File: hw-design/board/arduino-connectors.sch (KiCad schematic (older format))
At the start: 11 parts, among them P1 CONN_01X08, P2 CONN_01X06, P3 CONN_01X10, P4 CONN_01X08, Q1 2N7002

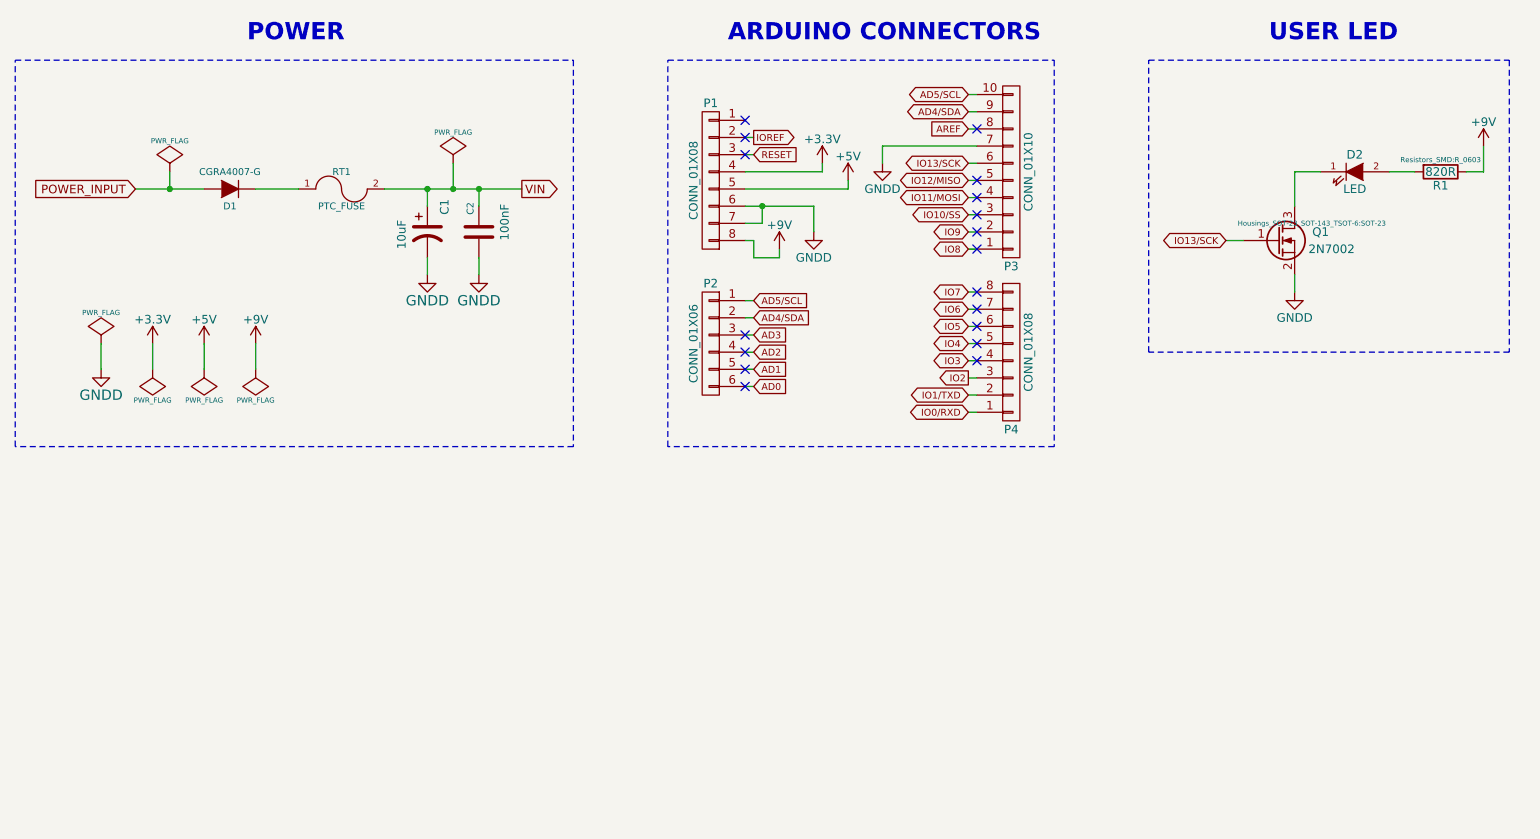
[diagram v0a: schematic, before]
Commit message: sch: setting up footprints
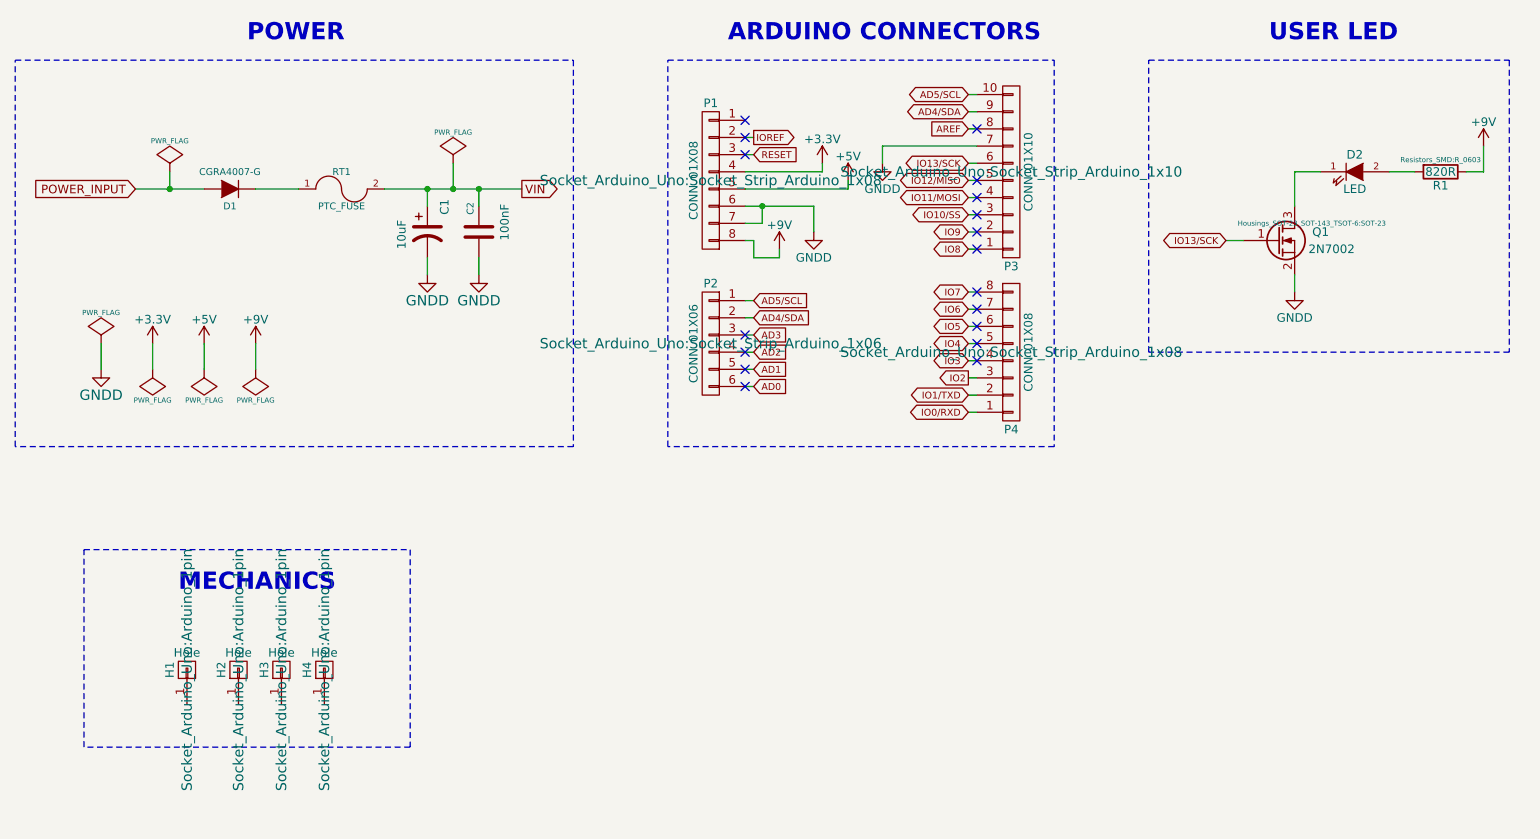
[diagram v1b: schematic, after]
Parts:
- added H1, H2, H3, H4: Hole, Socket_Arduino_Uno:Arduino_1pin, symbol CONN_01X01
- P1, P4: footprint (none) -> Socket_Arduino_Uno:Socket_Strip_Arduino_1x08
- P2: footprint (none) -> Socket_Arduino_Uno:Socket_Strip_Arduino_1x06
- P3: footprint (none) -> Socket_Arduino_Uno:Socket_Strip_Arduino_1x10
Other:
- note added: "MECHANICS"
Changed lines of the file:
@@
 	2800 2050 3050 2050
 Wire Wire Line
-	2100 2050 2300 2050
-Wire Wire Line
-	2300 2050 2500 2050
+	2100 2050 2500 2050
 Wire Wire Line
 	1900 2950 1900 3100
@@
 VIN
 Wire Wire Line
-	3550 2050 3800 2050
-Wire Wire Line
-	3800 2050 3950 2050
-Wire Wire Line
-	3950 2050 4100 2050
-Wire Wire Line
-	4100 2050 4350 2050
+	3550 2050 4350 2050
 NoConn ~ 5650 1650
 Text GLabel 5700 3200 2    40   Input ~ 0
@@
 F 0 "P1" H 5450 2450 50  0000 C CNN
 F 1 "CONN_01X08" V 5550 2000 50  0000 C CNN
-F 2 "" H 5450 2000 60  0000 C CNN
+F 2 "Socket_Arduino_Uno:Socket_Strip_Arduino_1x08" H 5450 2000 60  0000 C CNN
 F 3 "" H 5450 2000 60  0000 C CNN
 	1    5450 2000
@@
 F 0 "P2" H 5450 3300 50  0000 C CNN
 F 1 "CONN_01X06" V 5550 2950 50  0000 C CNN
-F 2 "" H 5450 2950 60  0000 C CNN
+F 2 "Socket_Arduino_Uno:Socket_Strip_Arduino_1x06" H 5450 2950 60  0000 C CNN
 F 3 "" H 5450 2950 60  0000 C CNN
 	1    5450 2950
@@
 F 0 "P3" H 7200 2500 50  0000 C CNN
 F 1 "CONN_01X10" V 7300 1950 50  0000 C CNN
-F 2 "" H 7200 1950 60  0000 C CNN
+F 2 "Socket_Arduino_Uno:Socket_Strip_Arduino_1x10" H 7200 1950 60  0000 C CNN
 F 3 "" H 7200 1950 60  0000 C CNN
 	1    7200 1950
@@
 F 0 "P4" H 7200 3450 50  0000 C CNN
 F 1 "CONN_01X08" V 7300 3000 50  0000 C CNN
-F 2 "" H 7200 3000 60  0000 C CNN
+F 2 "Socket_Arduino_Uno:Socket_Strip_Arduino_1x08" H 7200 3000 60  0000 C CNN
 F 3 "" H 7200 3000 60  0000 C CNN
 	1    7200 3000
@@
 	6050 2150 6050 2300
 Wire Wire Line
-	5650 2150 5750 2150
-Wire Wire Line
-	5750 2150 6050 2150
+	5650 2150 6050 2150
 Wire Wire Line
 	5650 2250 5750 2250
@@
 Wire Wire Line
 	6100 1950 6100 1900
+Text Notes 2350 4400 0    100  ~ 20
+MECHANICS
+$Comp
+L CONN_01X01 H1
+U 1 1 558C38D7
+P 2400 4850
+F 0 "H1" H 2400 4950 50  0000 C CNN
+F 1 "Hole" V 2500 4850 50  0000 C CNN
+F 2 "Socket_Arduino_Uno:Arduino_1pin" H 2400 4850 60  0000 C CNN
+F 3 "" H 2400 4850 60  0000 C CNN
+	1    2400 4850
+	0    -1   -1   0
+$EndComp
+$Comp
+L CONN_01X01 H2
+U 1 1 558C3F79
+P 2700 4850
+F 0 "H2" H 2700 4950 50  0000 C CNN
+F 1 "Hole" V 2800 4850 50  0000 C CNN
+F 2 "Socket_Arduino_Uno:Arduino_1pin" H 2700 4850 60  0000 C CNN
+F 3 "" H 2700 4850 60  0000 C CNN
+	1    2700 4850
+	0    -1   -1   0
+$EndComp
+$Comp
+L CONN_01X01 H3
+U 1 1 558C3FB1
+P 2950 4850
+F 0 "H3" H 2950 4950 50  0000 C CNN
+F 1 "Hole" V 3050 4850 50  0000 C CNN
+F 2 "Socket_Arduino_Uno:Arduino_1pin" H 2950 4850 60  0000 C CNN
+F 3 "" H 2950 4850 60  0000 C CNN
+	1    2950 4850
+	0    -1   -1   0
+$EndComp
+$Comp
+L CONN_01X01 H4
+U 1 1 558C3FE5
+P 3200 4850
+F 0 "H4" H 3200 4950 50  0000 C CNN
+F 1 "Hole" V 3300 4850 50  0000 C CNN
+F 2 "Socket_Arduino_Uno:Arduino_1pin" H 3200 4850 60  0000 C CNN
+F 3 "" H 3200 4850 60  0000 C CNN
+	1    3200 4850
+	0    -1   -1   0
+$EndComp
+Wire Notes Line
+	1800 4150 3700 4150
+Wire Notes Line
+	3700 4150 3700 5300
+Wire Notes Line
+	3700 5300 1800 5300
+Wire Notes Line
+	1800 5300 1800 4150
 $EndSCHEMATC

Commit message: adding footprint to local project directory (submodule)
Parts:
- D2: footprint (none) -> LEDs:LED-0603; MPN (none) -> LS Q976-NR-1
- P1: value CONN_01X08 -> Power
- P2: value CONN_01X06 -> Analog
- P3: value CONN_01X10 -> Digital
- P4: value CONN_01X08 -> Digital
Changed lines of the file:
@@
 U 1 1 548B665F
 P 4100 2300
-F 0 "C2" V 4050 2400 40  0000 L CNN
+F 0 "C2" V 4050 2400 50  0000 L CNN
 F 1 "100nF" V 4250 2250 50  0000 L CNN
 F 2 "Capacitors_SMD:C_0603" H 4138 2150 30  0001 C CNN
@@
 P 5450 2000
 F 0 "P1" H 5450 2450 50  0000 C CNN
-F 1 "CONN_01X08" V 5550 2000 50  0000 C CNN
-F 2 "Socket_Arduino_Uno:Socket_Strip_Arduino_1x08" H 5450 2000 60  0000 C CNN
+F 1 "Power" V 5550 2000 50  0000 C CNN
+F 2 "Socket_Arduino_Uno:Socket_Strip_Arduino_1x08" V 5450 2000 60  0001 C CNN
 F 3 "" H 5450 2000 60  0000 C CNN
 	1    5450 2000
@@
 P 5450 2950
 F 0 "P2" H 5450 3300 50  0000 C CNN
-F 1 "CONN_01X06" V 5550 2950 50  0000 C CNN
-F 2 "Socket_Arduino_Uno:Socket_Strip_Arduino_1x06" H 5450 2950 60  0000 C CNN
+F 1 "Analog" V 5550 2950 50  0000 C CNN
+F 2 "Socket_Arduino_Uno:Socket_Strip_Arduino_1x06" V 5450 2950 60  0001 C CNN
 F 3 "" H 5450 2950 60  0000 C CNN
 	1    5450 2950
@@
 P 7200 1950
 F 0 "P3" H 7200 2500 50  0000 C CNN
-F 1 "CONN_01X10" V 7300 1950 50  0000 C CNN
-F 2 "Socket_Arduino_Uno:Socket_Strip_Arduino_1x10" H 7200 1950 60  0000 C CNN
+F 1 "Digital" V 7300 1950 50  0000 C CNN
+F 2 "Socket_Arduino_Uno:Socket_Strip_Arduino_1x10" V 7200 1950 60  0001 C CNN
 F 3 "" H 7200 1950 60  0000 C CNN
 	1    7200 1950
@@
 P 7200 3000
 F 0 "P4" H 7200 3450 50  0000 C CNN
-F 1 "CONN_01X08" V 7300 3000 50  0000 C CNN
-F 2 "Socket_Arduino_Uno:Socket_Strip_Arduino_1x08" H 7200 3000 60  0000 C CNN
+F 1 "Digital" V 7300 3000 50  0000 C CNN
+F 2 "Socket_Arduino_Uno:Socket_Strip_Arduino_1x08" V 7200 3000 60  0001 C CNN
 F 3 "" H 7200 3000 60  0000 C CNN
 	1    7200 3000
@@
 F 0 "Q1" H 9050 2400 50  0000 R CNN
 F 1 "2N7002" H 9200 2300 50  0000 R CNN
-F 2 "Housings_SOT-23_SOT-143_TSOT-6:SOT-23" H 8950 2450 29  0000 C CNN
+F 2 "Housings_SOT-23_SOT-143_TSOT-6:SOT-23" H 8950 2450 50  0000 C CNN
 F 3 "" H 8750 2350 60  0000 C CNN
 F 4 "2N7002P,215" H 8750 2350 60  0001 C CNN "MPN"
@@
 F 0 "D2" H 9200 2050 50  0000 C CNN
 F 1 "LED" H 9200 1850 50  0000 C CNN
-F 2 "" H 9200 1950 60  0000 C CNN
+F 2 "LEDs:LED-0603" H 9200 2150 50  0000 C CNN
 F 3 "" H 9200 1950 60  0000 C CNN
+F 4 "LS Q976-NR-1" H 9200 1950 60  0001 C CNN "MPN"
 	1    9200 1950
 	1    0    0    -1
@@
 F 0 "R1" V 9780 1950 50  0000 C CNN
 F 1 "820R" V 9700 1950 50  0000 C CNN
-F 2 "Resistors_SMD:R_0603" V 9630 1950 30  0000 C CNN
+F 2 "Resistors_SMD:R_0603" V 9630 1950 50  0000 C CNN
 F 3 "" H 9700 1950 30  0000 C CNN
 F 4 "ESR03EZPJ821" V 9700 1950 60  0001 C CNN "MPN"
@@
 	5850 2450 5850 2400
 $Comp
-L +5V #PWR?
+L +5V #PWR018
 U 1 1 558D2AB4
 P 6250 2000
-F 0 "#PWR?" H 6250 1850 50  0001 C CNN
+F 0 "#PWR018" H 6250 1850 50  0001 C CNN
 F 1 "+5V" H 6250 2140 50  0000 C CNN
 F 2 "" H 6250 2000 60  0000 C CNN
@@
 	6250 2050 6250 2000
 $Comp
-L +3.3V #PWR?
+L +3.3V #PWR019
 U 1 1 558D2EDB
 P 6100 1900
-F 0 "#PWR?" H 6100 1750 50  0001 C CNN
+F 0 "#PWR019" H 6100 1750 50  0001 C CNN
 F 1 "+3.3V" H 6100 2040 50  0000 C CNN
 F 2 "" H 6100 1900 60  0000 C CNN
@@
 F 0 "H1" H 2400 4950 50  0000 C CNN
 F 1 "Hole" V 2500 4850 50  0000 C CNN
-F 2 "Socket_Arduino_Uno:Arduino_1pin" H 2400 4850 60  0000 C CNN
+F 2 "Socket_Arduino_Uno:Arduino_1pin" H 2400 4850 60  0001 C CNN
 F 3 "" H 2400 4850 60  0000 C CNN
 	1    2400 4850
@@
 F 0 "H2" H 2700 4950 50  0000 C CNN
 F 1 "Hole" V 2800 4850 50  0000 C CNN
-F 2 "Socket_Arduino_Uno:Arduino_1pin" H 2700 4850 60  0000 C CNN
+F 2 "Socket_Arduino_Uno:Arduino_1pin" H 2700 4850 60  0001 C CNN
 F 3 "" H 2700 4850 60  0000 C CNN
 	1    2700 4850
@@
 F 0 "H3" H 2950 4950 50  0000 C CNN
 F 1 "Hole" V 3050 4850 50  0000 C CNN
-F 2 "Socket_Arduino_Uno:Arduino_1pin" H 2950 4850 60  0000 C CNN
+F 2 "Socket_Arduino_Uno:Arduino_1pin" H 2950 4850 60  0001 C CNN
 F 3 "" H 2950 4850 60  0000 C CNN
 	1    2950 4850
@@
 F 0 "H4" H 3200 4950 50  0000 C CNN
 F 1 "Hole" V 3300 4850 50  0000 C CNN
-F 2 "Socket_Arduino_Uno:Arduino_1pin" H 3200 4850 60  0000 C CNN
+F 2 "Socket_Arduino_Uno:Arduino_1pin" H 3200 4850 60  0001 C CNN
 F 3 "" H 3200 4850 60  0000 C CNN
 	1    3200 4850

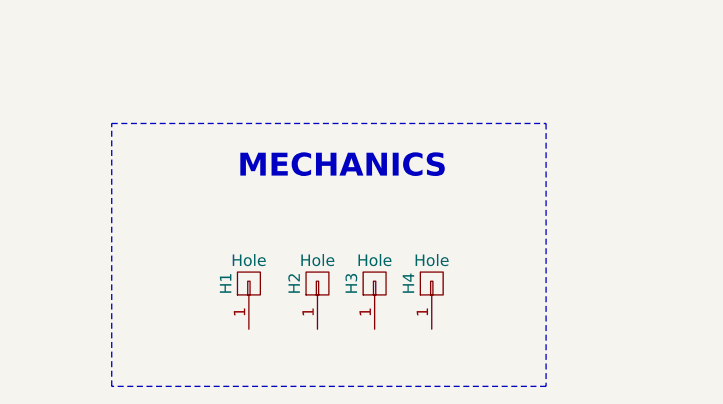
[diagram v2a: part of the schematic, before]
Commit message: sch: fixing footprints and renaming some connectors
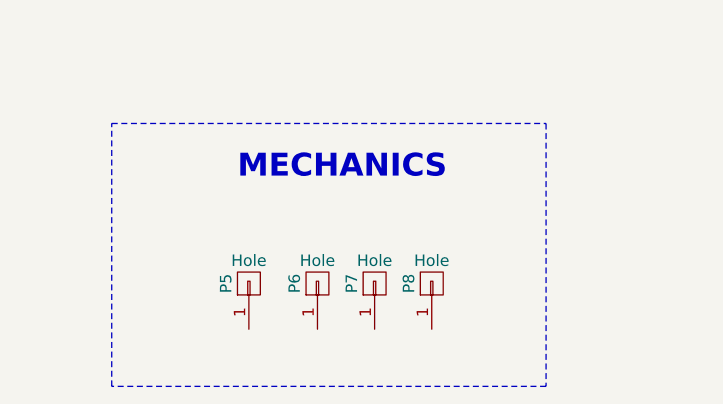
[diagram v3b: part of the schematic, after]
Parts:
- renumbered H1 to P5, H2 to P6, H3 to P7, H4 to P8
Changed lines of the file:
@@
 $EndComp
 $Comp
-L PWR_FLAG #FLG01
+L PWR_FLAG #FLG1
 U 1 1 54B500E8
 P 1900 2950
-F 0 "#FLG01" H 1900 3045 30  0001 C CNN
+F 0 "#FLG1" H 1900 3045 30  0001 C CNN
 F 1 "PWR_FLAG" H 1900 3130 30  0000 C CNN
 F 2 "" H 1900 2950 60  0000 C CNN
@@
 $EndComp
 $Comp
-L PWR_FLAG #FLG02
+L PWR_FLAG #FLG3
 U 1 1 54B50E4C
 P 2300 1950
-F 0 "#FLG02" H 2300 2045 30  0001 C CNN
+F 0 "#FLG3" H 2300 2045 30  0001 C CNN
 F 1 "PWR_FLAG" H 2300 2130 30  0000 C CNN
 F 2 "" H 2300 1950 60  0000 C CNN
@@
 $EndComp
 $Comp
-L GNDD #PWR03
+L GNDD #PWR1
 U 1 1 54E7EDE1
 P 1900 3100
-F 0 "#PWR03" H 1900 2850 60  0001 C CNN
+F 0 "#PWR1" H 1900 2850 60  0001 C CNN
 F 1 "GNDD" H 1900 2950 60  0000 C CNN
 F 2 "" H 1900 3100 60  0000 C CNN
@@
 $EndComp
 $Comp
-L GNDD #PWR04
+L GNDD #PWR5
 U 1 1 54E7EE6C
 P 3800 2550
-F 0 "#PWR04" H 3800 2300 60  0001 C CNN
+F 0 "#PWR5" H 3800 2300 60  0001 C CNN
 F 1 "GNDD" H 3800 2400 60  0000 C CNN
 F 2 "" H 3800 2550 60  0000 C CNN
@@
 $EndComp
 $Comp
-L GNDD #PWR05
+L GNDD #PWR6
 U 1 1 54E7EE80
 P 4100 2550
-F 0 "#PWR05" H 4100 2300 60  0001 C CNN
+F 0 "#PWR6" H 4100 2300 60  0001 C CNN
 F 1 "GNDD" H 4100 2400 60  0000 C CNN
 F 2 "" H 4100 2550 60  0000 C CNN
@@
 $EndComp
 $Comp
-L PWR_FLAG #FLG06
+L PWR_FLAG #FLG6
 U 1 1 557B2C54
 P 3950 1900
-F 0 "#FLG06" H 3950 1995 30  0001 C CNN
+F 0 "#FLG6" H 3950 1995 30  0001 C CNN
 F 1 "PWR_FLAG" H 3950 2080 30  0000 C CNN
 F 2 "" H 3950 1900 60  0000 C CNN
@@
 $EndComp
 $Comp
-L PWR_FLAG #FLG07
+L PWR_FLAG #FLG4
 U 1 1 557B3123
 P 2500 3100
-F 0 "#FLG07" H 2500 3195 30  0001 C CNN
+F 0 "#FLG4" H 2500 3195 30  0001 C CNN
 F 1 "PWR_FLAG" H 2500 3280 30  0000 C CNN
 F 2 "" H 2500 3100 60  0000 C CNN
@@
 $EndComp
 $Comp
-L +5V #PWR08
+L +5V #PWR3
 U 1 1 557B3200
 P 2500 2950
-F 0 "#PWR08" H 2500 2800 50  0001 C CNN
+F 0 "#PWR3" H 2500 2800 50  0001 C CNN
 F 1 "+5V" H 2500 3090 50  0000 C CNN
 F 2 "" H 2500 2950 60  0000 C CNN
@@
 $EndComp
 $Comp
-L PWR_FLAG #FLG09
+L PWR_FLAG #FLG5
 U 1 1 557B4378
 P 2800 3100
-F 0 "#FLG09" H 2800 3195 30  0001 C CNN
+F 0 "#FLG5" H 2800 3195 30  0001 C CNN
 F 1 "PWR_FLAG" H 2800 3280 30  0000 C CNN
 F 2 "" H 2800 3100 60  0000 C CNN
@@
 $EndComp
 $Comp
-L +9V #PWR010
+L +9V #PWR4
 U 1 1 557B43C7
 P 2800 2950
-F 0 "#PWR010" H 2800 2800 50  0001 C CNN
+F 0 "#PWR4" H 2800 2800 50  0001 C CNN
 F 1 "+9V" H 2800 3090 50  0000 C CNN
 F 2 "" H 2800 2950 60  0000 C CNN
@@
 $EndComp
 $Comp
-L GNDD #PWR011
+L GNDD #PWR12
 U 1 1 558C6089
 P 8850 2650
-F 0 "#PWR011" H 8850 2400 50  0001 C CNN
+F 0 "#PWR12" H 8850 2400 50  0001 C CNN
 F 1 "GNDD" H 8850 2500 50  0000 C CNN
 F 2 "" H 8850 2650 60  0000 C CNN
@@
 	9550 1950 9400 1950
 $Comp
-L +9V #PWR012
+L +9V #PWR13
 U 1 1 558C6BA4
 P 9950 1800
-F 0 "#PWR012" H 9950 1650 50  0001 C CNN
+F 0 "#PWR13" H 9950 1650 50  0001 C CNN
 F 1 "+9V" H 9950 1940 50  0000 C CNN
 F 2 "" H 9950 1800 60  0000 C CNN
@@
 	8000 3000 8000 1300
 $Comp
-L PWR_FLAG #FLG013
+L PWR_FLAG #FLG2
 U 1 1 558CC3E6
 P 2200 3100
-F 0 "#FLG013" H 2200 3195 30  0001 C CNN
+F 0 "#FLG2" H 2200 3195 30  0001 C CNN
 F 1 "PWR_FLAG" H 2200 3280 30  0000 C CNN
 F 2 "" H 2200 3100 60  0000 C CNN
@@
 	2200 2950 2200 3100
 $Comp
-L +3.3V #PWR014
+L +3.3V #PWR2
 U 1 1 558CC417
 P 2200 2950
-F 0 "#PWR014" H 2200 2800 50  0001 C CNN
+F 0 "#PWR2" H 2200 2800 50  0001 C CNN
 F 1 "+3.3V" H 2200 3090 50  0000 C CNN
 F 2 "" H 2200 2950 60  0000 C CNN
@@
 NoConn ~ 7000 1700
 $Comp
-L GNDD #PWR015
+L GNDD #PWR11
 U 1 1 558D1E0A
 P 6450 1900
-F 0 "#PWR015" H 6450 1650 50  0001 C CNN
+F 0 "#PWR11" H 6450 1650 50  0001 C CNN
 F 1 "GNDD" H 6450 1750 50  0000 C CNN
 F 2 "" H 6450 1900 60  0000 C CNN
@@
 	6450 1800 7000 1800
 $Comp
-L GNDD #PWR016
+L GNDD #PWR8
 U 1 1 558D2084
 P 6050 2300
-F 0 "#PWR016" H 6050 2050 50  0001 C CNN
+F 0 "#PWR8" H 6050 2050 50  0001 C CNN
 F 1 "GNDD" H 6050 2150 50  0000 C CNN
 F 2 "" H 6050 2300 60  0000 C CNN
@@
 Connection ~ 5750 2150
 $Comp
-L +9V #PWR017
+L +9V #PWR7
 U 1 1 558D2217
 P 5850 2400
-F 0 "#PWR017" H 5850 2250 50  0001 C CNN
+F 0 "#PWR7" H 5850 2250 50  0001 C CNN
 F 1 "+9V" H 5850 2540 50  0000 C CNN
 F 2 "" H 5850 2400 60  0000 C CNN
@@
 	5850 2450 5850 2400
 $Comp
-L +5V #PWR018
+L +5V #PWR10
 U 1 1 558D2AB4
 P 6250 2000
-F 0 "#PWR018" H 6250 1850 50  0001 C CNN
+F 0 "#PWR10" H 6250 1850 50  0001 C CNN
 F 1 "+5V" H 6250 2140 50  0000 C CNN
 F 2 "" H 6250 2000 60  0000 C CNN
@@
 	6250 2050 6250 2000
 $Comp
-L +3.3V #PWR019
+L +3.3V #PWR9
 U 1 1 558D2EDB
 P 6100 1900
-F 0 "#PWR019" H 6100 1750 50  0001 C CNN
+F 0 "#PWR9" H 6100 1750 50  0001 C CNN
 F 1 "+3.3V" H 6100 2040 50  0000 C CNN
 F 2 "" H 6100 1900 60  0000 C CNN
@@
 MECHANICS
 $Comp
-L CONN_01X01 H1
+L CONN_01X01 P5
 U 1 1 558C38D7
 P 2400 4850
-F 0 "H1" H 2400 4950 50  0000 C CNN
+F 0 "P5" H 2400 4950 50  0000 C CNN
 F 1 "Hole" V 2500 4850 50  0000 C CNN
 F 2 "Socket_Arduino_Uno:Arduino_1pin" H 2400 4850 60  0001 C CNN
@@
 $EndComp
 $Comp
-L CONN_01X01 H2
+L CONN_01X01 P6
 U 1 1 558C3F79
 P 2700 4850
-F 0 "H2" H 2700 4950 50  0000 C CNN
+F 0 "P6" H 2700 4950 50  0000 C CNN
 F 1 "Hole" V 2800 4850 50  0000 C CNN
 F 2 "Socket_Arduino_Uno:Arduino_1pin" H 2700 4850 60  0001 C CNN
@@
 $EndComp
 $Comp
-L CONN_01X01 H3
+L CONN_01X01 P7
 U 1 1 558C3FB1
 P 2950 4850
-F 0 "H3" H 2950 4950 50  0000 C CNN
+F 0 "P7" H 2950 4950 50  0000 C CNN
 F 1 "Hole" V 3050 4850 50  0000 C CNN
 F 2 "Socket_Arduino_Uno:Arduino_1pin" H 2950 4850 60  0001 C CNN
@@
 $EndComp
 $Comp
-L CONN_01X01 H4
+L CONN_01X01 P8
 U 1 1 558C3FE5
 P 3200 4850
-F 0 "H4" H 3200 4950 50  0000 C CNN
+F 0 "P8" H 3200 4950 50  0000 C CNN
 F 1 "Hole" V 3300 4850 50  0000 C CNN
 F 2 "Socket_Arduino_Uno:Arduino_1pin" H 3200 4850 60  0001 C CNN
